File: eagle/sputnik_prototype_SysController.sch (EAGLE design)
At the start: 60 parts, among them U1 MEGA128-A, X1 CRYSTAL-ABRACON-ABM3-SMD

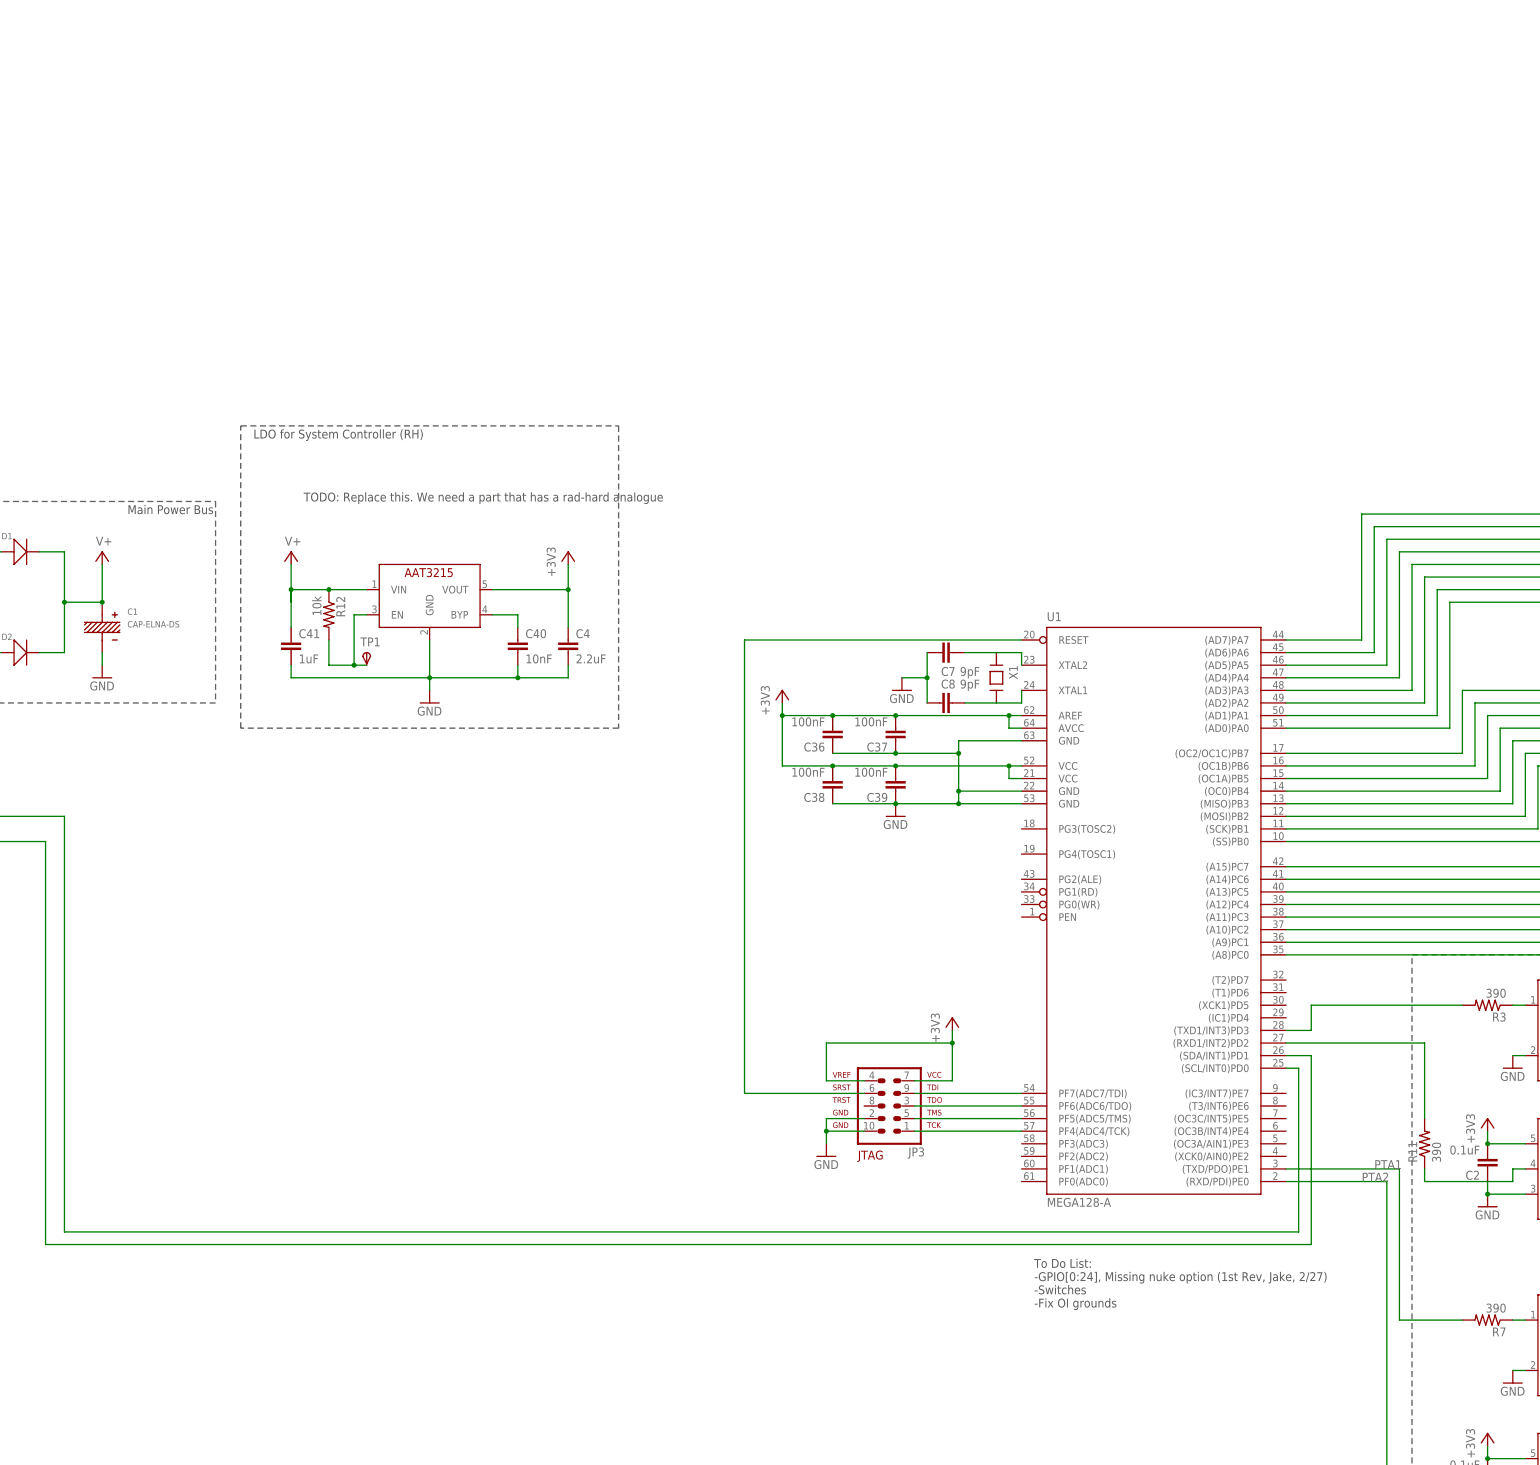
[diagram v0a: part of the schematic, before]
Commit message: Added the bare switch and deleted some text
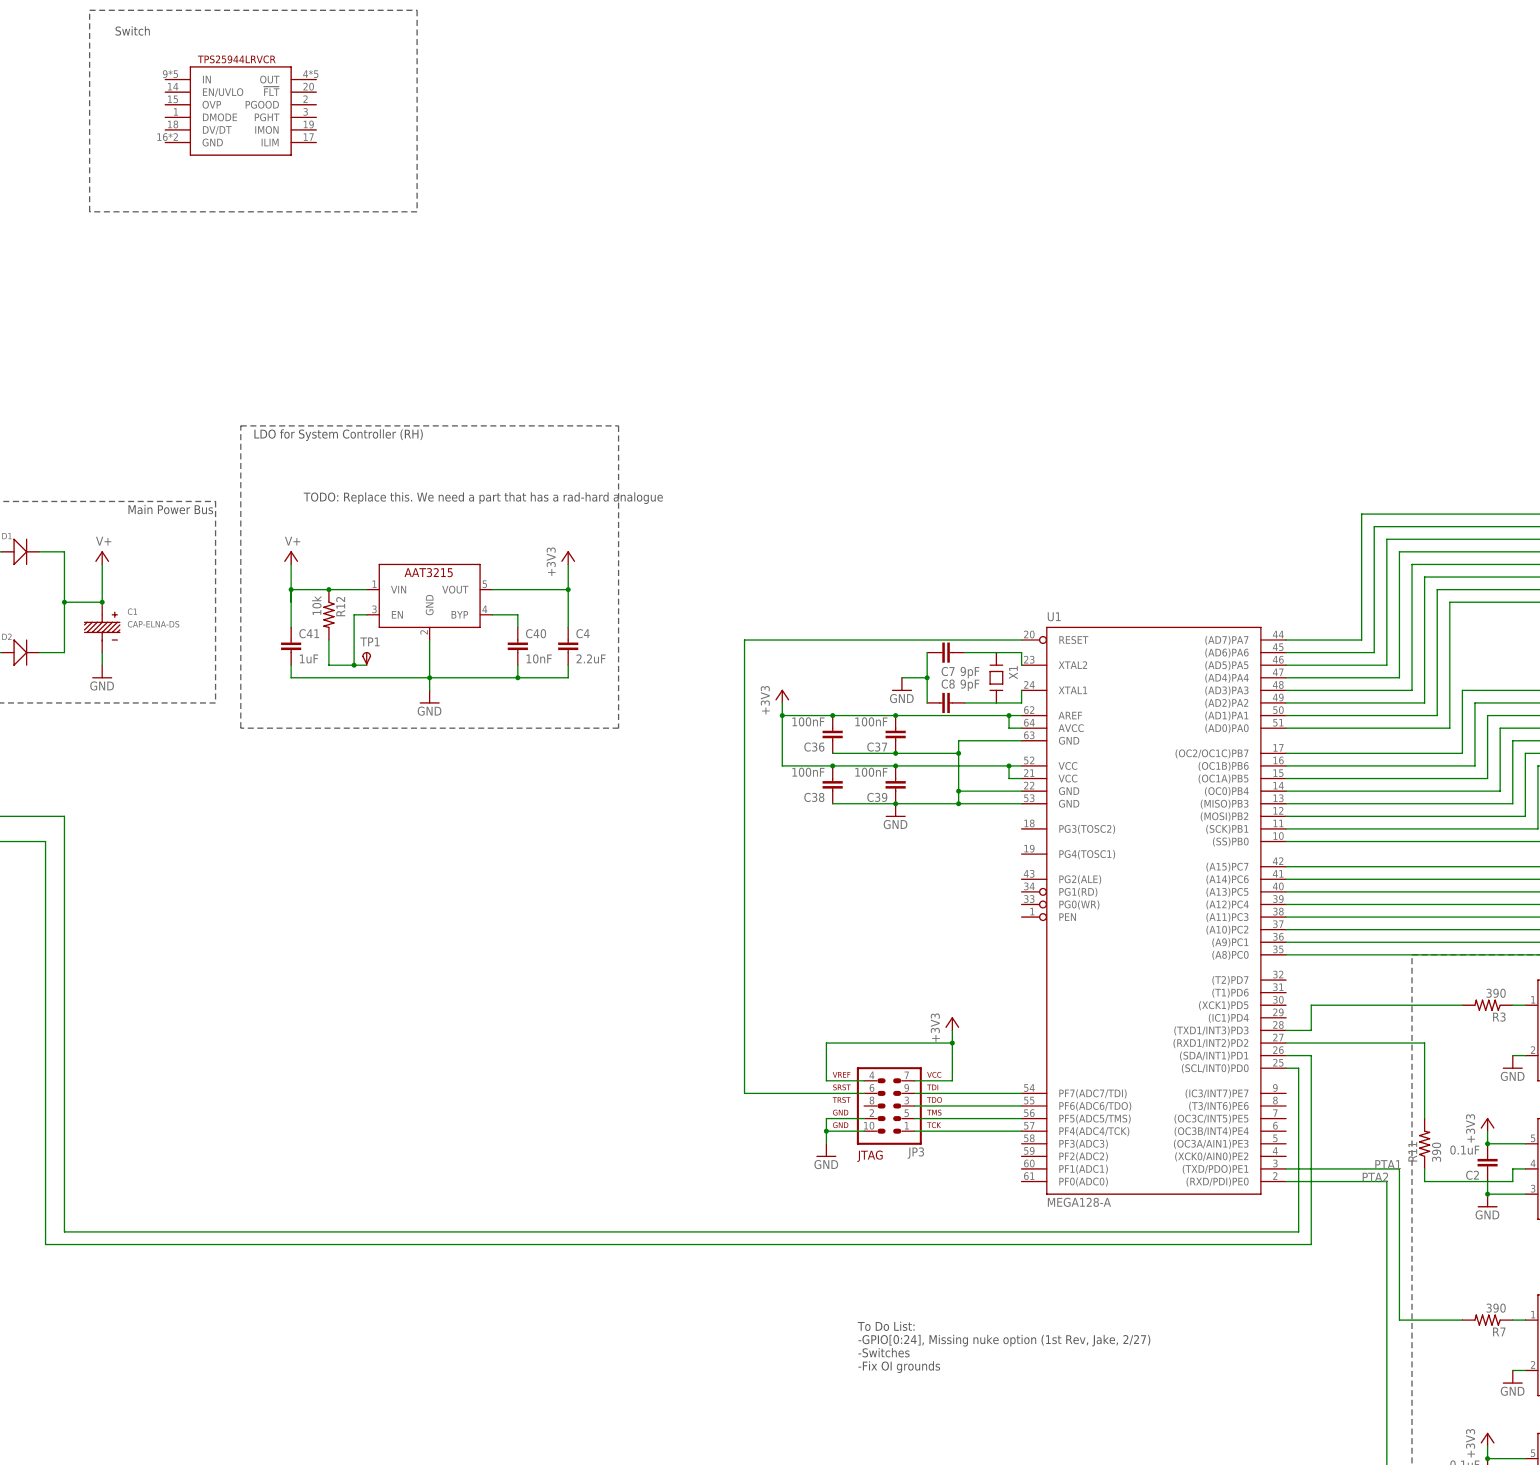
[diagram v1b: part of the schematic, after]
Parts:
- added SW1: TPS25944LRVCRWQFN-20-3X4, WQFN-20-3x4:TPS25944LRVCRWQFN-20-3X4
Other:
- note added: "Switch"
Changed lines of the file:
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@@
 <?xml version="1.0" encoding="utf-8"?>
 <!DOCTYPE eagle SYSTEM "eagle.dtd">
-<eagle version="7.3.0">
+<eagle version="7.4.0">
 <drawing>
 <settings>
@@
 <part name="+3V5" library="supply1" deviceset="+3V3" device=""/>
 <part name="CF2" library="oresat-eagle" deviceset="ORESAT-CONNECTOR-40PIN" device=""/>
+<part name="SW1" library="WQFN-20-3x4" deviceset="TPS25944LRVCR" device="WQFN-20-3X4"/>
 </parts>
 <sheets>
@@
 <wire x1="426.72" y1="200.66" x2="426.72" y2="307.34" width="0.1524" layer="97" style="longdash"/>
 <text x="429.26" y="304.8" size="1.778" layer="97">Power interface</text>
-<text x="284.48" y="134.62" size="1.778" layer="97">To Do List:
+<text x="248.92" y="121.92" size="1.778" layer="97">To Do List:
 -GPIO[0:24], Missing nuke option (1st Rev, Jake, 2/27)
 -Switches
@@
 8. ADS-Sunsensors
 9.ADS-Starfinder/Sunsensor</text>
+<wire x1="93.98" y1="396.24" x2="160.02" y2="396.24" width="0.1524" layer="97" style="longdash"/>
+<wire x1="160.02" y1="396.24" x2="160.02" y2="355.6" width="0.1524" layer="97" style="longdash"/>
+<wire x1="160.02" y1="355.6" x2="93.98" y2="355.6" width="0.1524" layer="97" style="longdash"/>
+<wire x1="93.98" y1="355.6" x2="93.98" y2="396.24" width="0.1524" layer="97" style="longdash"/>
+<text x="99.06" y="391.16" size="1.778" layer="97">Switch</text>
 </plain>
 <instances>
@@
 <attribute name="VALUE" x="505.46" y="236.22" size="1.778" layer="96" rot="MR90"/>
 </instance>
+<instance part="SW1" gate="G$1" x="124.46" y="375.92"/>
 </instances>
 <busses>

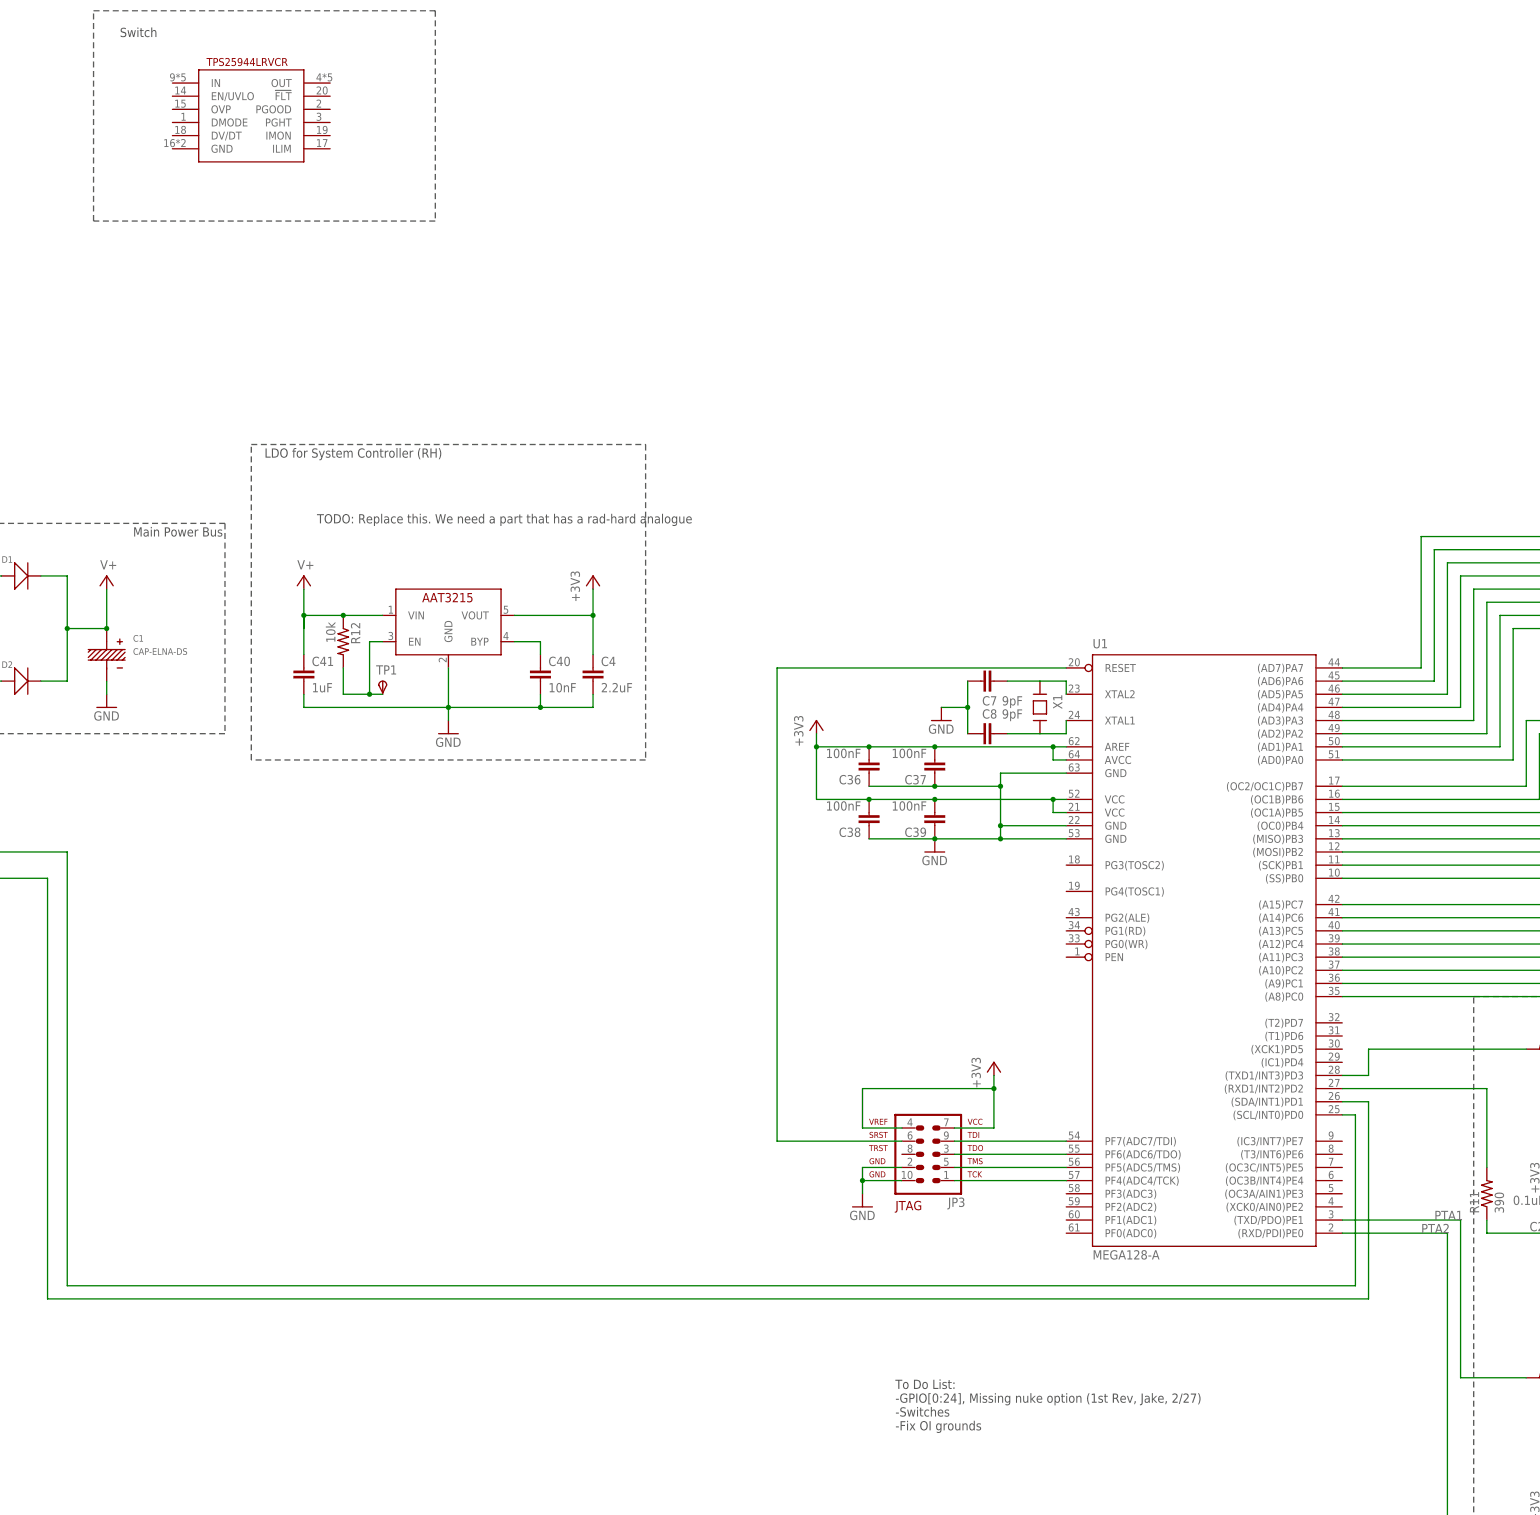
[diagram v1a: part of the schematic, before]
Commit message: worked on the switch schematic
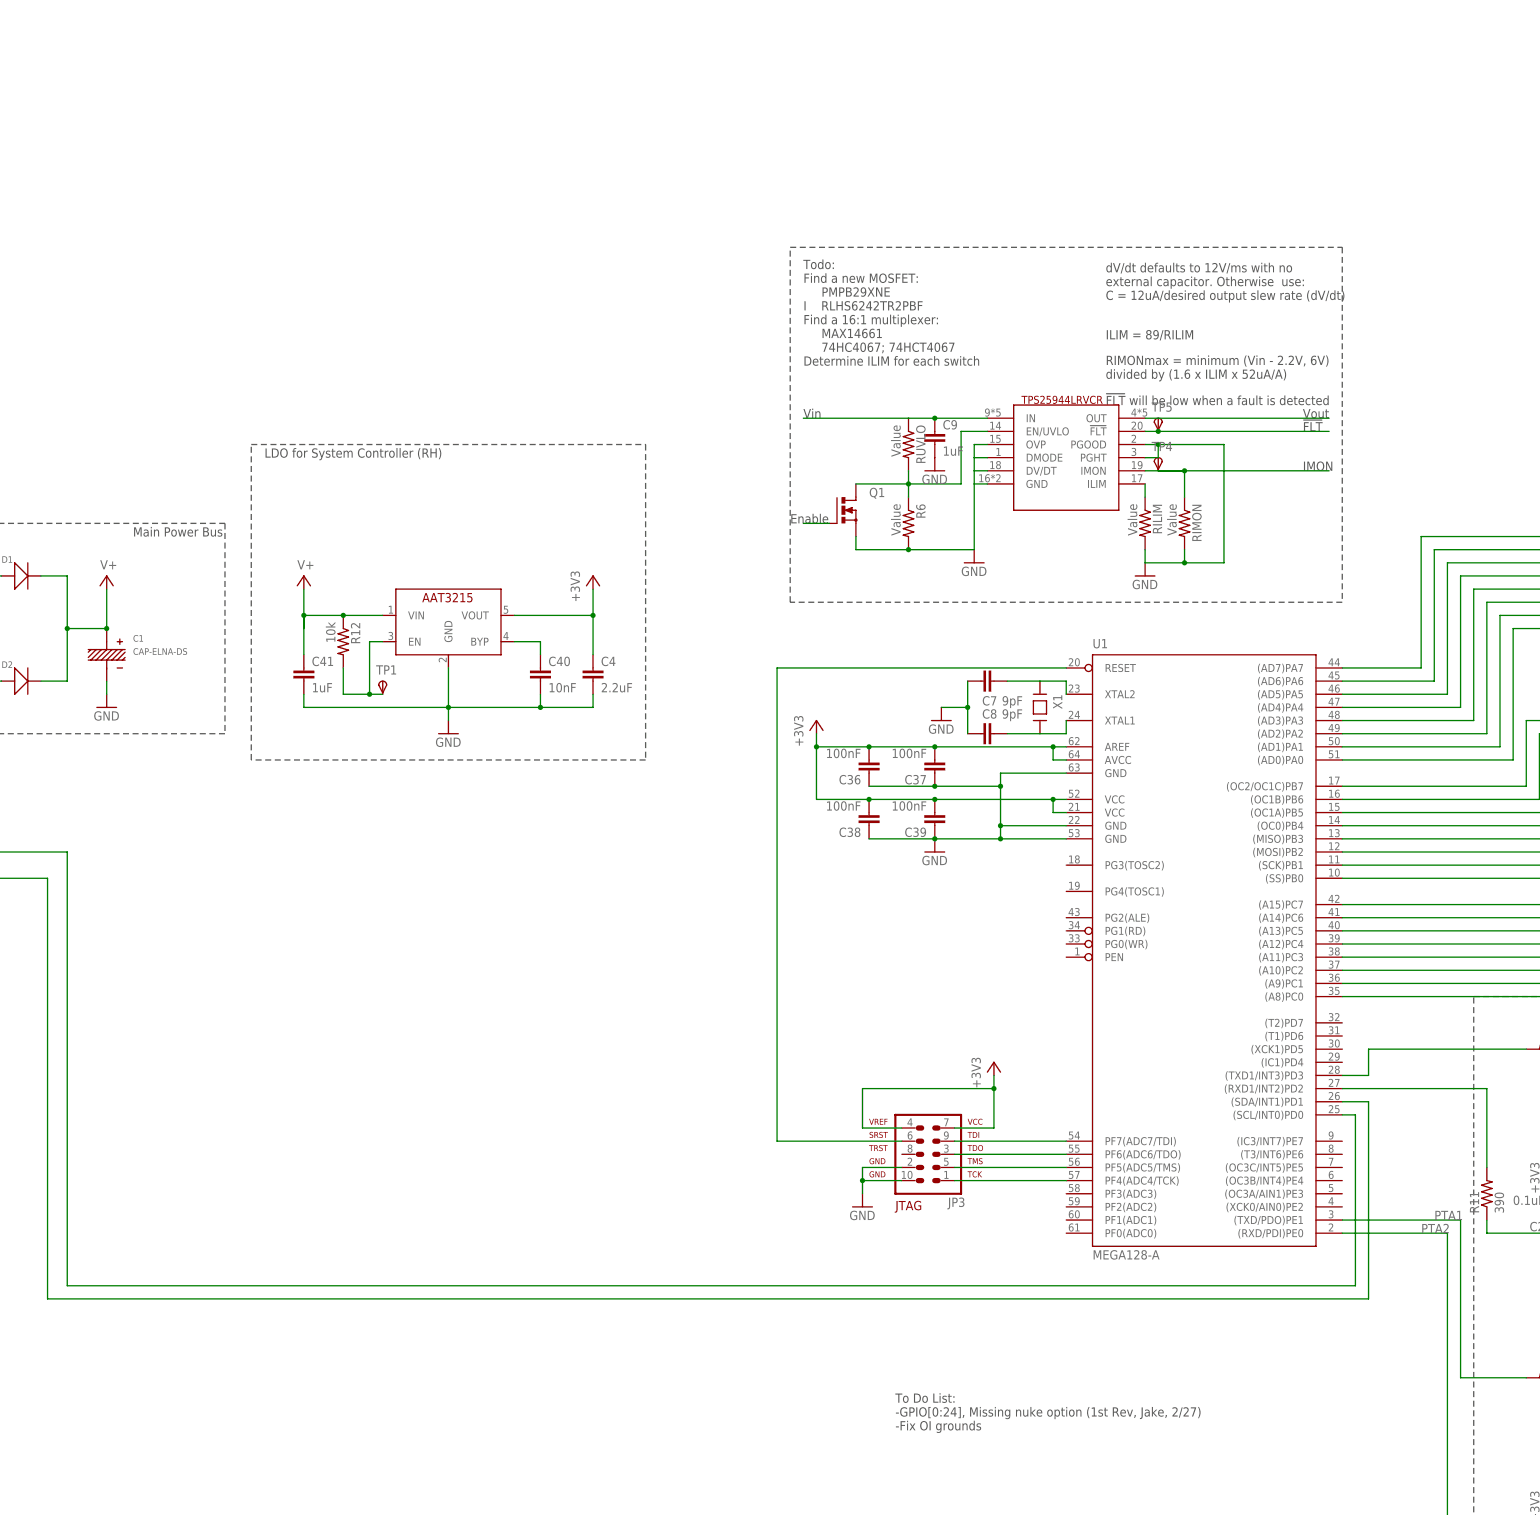
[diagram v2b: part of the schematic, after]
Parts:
- added C9: 1uF, rcl_custom:C-EU0402-B-NOSILK
- added Q1: (no value), transistor-power:N-MOSFET-SO8S
- added R6, RILIM, RIMON, RUVLO: Value, rcl_custom:R-US_0603-B-NOSILK
- added TP4, TP5: TPSPAD1-13, testpad:TPSPAD1-13
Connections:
- new net N$2: C9.1, RUVLO.1, SW1.IN
- new net N$21: RILIM.1, SW1.ILIM
- new net N$26: Q1.G
- new net N$27: RIMON.1, SW1.IMON, TP4.PP
- new net N$3: SW1.OUT
- new net N$7: SW1.!FLT, TP5.PP
- new net N$9: Q1.D, R6.1, RUVLO.2, SW1.EN/UVLO
- net GND: now also C9.2, Q1.S, R6.2, RILIM.2, RIMON.2, SW1.DMODE, SW1.DV/DT, SW1.GND, SW1.OVP, SW1.PGHT, SW1.PGOOD
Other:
- note added: "!FLT"
- note added: "!FLT! will be low when a fault is detected"
- note added: "Enable"
- note added: "ILIM = 89/RILIM"
- note added: "IMON"
- note added: "RIMONmax = minimum (Vin - 2.2V, 6V) divided by (1.6 x ILIM x 52uA/A)"
- note added: "To Do List: -GPIO[0:24], Missing nuke option (1st Rev, Jake, 2/27) -Fix OI grounds"
- note added: "Todo: Find a new MOSFET: PMPB29XNE I RLHS6242TR2PBF Find a 16:1 multiplexer: MAX14661 74HC4067; 74HCT4067 Determine ILIM for each switch"
- note added: "Vin"
- note added: "Vout"
- note added: "dV/dt defaults to 12V/ms with no external capacitor. Otherwise use: C = 12uA/desired output slew rate (dV/dt)"
- note removed: "Switch"
- note removed: "TODO: Replace this. We need a part that has a rad-hard analogue"
- note removed: "To Do List: -GPIO[0:24], Missing nuke option (1st Rev, Jake, 2/27) -Switches -Fix OI grounds"
